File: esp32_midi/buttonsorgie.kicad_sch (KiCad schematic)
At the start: 199 parts, among them SW10 SW_SPST, SW11 SW_SPST, SW12 SW_SPST, SW13 SW_SPST, SW14 SW_SPST, SW15 SW_SPST, SW16 SW_SPST, SW17 SW_SPST, SW18 SW_SPST, SW19 SW_SPST, SW2 SW_SPST, SW20 SW_SPST, SW21 SW_SPST, SW22 SW_SPST, SW23 SW_SPST, SW24 SW_SPST, SW25 SW_SPST, SW26 SW_SPST, SW27 SW_SPST, SW28 SW_SPST, SW29 SW_SPST, SW3 SW_SPST, SW30 SW_SPST, SW31 SW_SPST, SW32 SW_SPST, SW33 SW_SPST, SW34 SW_SPST, SW35 SW_SPST, SW36 SW_SPST, SW37 SW_SPST, SW38 SW_SPST, SW39 SW_SPST, SW4 SW_SPST, SW40 SW_SPST, SW41 SW_SPST, SW42 SW_SPST, SW43 SW_SPST, SW44 SW_SPST, SW45 SW_SPST, SW46 SW_SPST, SW47 SW_SPST, SW48 SW_SPST, SW49 SW_SPST, SW5 SW_SPST, SW50 SW_SPST, SW51 SW_SPST, SW52 SW_SPST, SW53 SW_SPST, SW54 SW_SPST, SW55 SW_SPST, SW56 SW_SPST, SW57 SW_SPST, SW58 SW_SPST, SW59 SW_SPST, SW6 SW_SPST, SW60 SW_SPST, SW61 SW_SPST, SW62 SW_SPST, SW63 SW_SPST, SW64 SW_SPST, SW65 SW_SPST, SW7 SW_SPST, SW8 SW_SPST, SW9 SW_SPST

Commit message: Started work on PCB
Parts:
- added R48, R49, R50: 10k, Resistor_SMD:R_0402_1005Metric, symbol Device:R
- added SW66, SW67, SW68, SW69, SW70, SW71, SW72, SW73: SW_SPST, ordentliche-teile:scheißbutton, symbol Switch:SW_SPST
- added SW74, SW75, SW76, SW77: SW_SPST, ordentliche-teile:bobbybutton, symbol Switch:SW_SPST
- added SW78, SW79, SW80, SW81: SW_SPST, Connector_PinSocket_2.54mm:PinSocket_1x02_P2.54mm_Vertical, symbol Switch:SW_SPST
- added U? (x4): USBLC6-4SC6, Package_TO_SOT_SMD:SOT-23-6, symbol Power_Protection:USBLC6-4SC6
- added U? (x35): BL1551, Package_TO_SOT_SMD:SOT-363_SC-70-6, symbol Analog_Switch:FSA3157L6X
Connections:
- net +3.3V: now also R48.1, R49.1, R50.1, U?.5 (V+), U?.5 (V+), U?.5 (V+), U?.5 (V+), U?.5 (V+), U?.5 (V+), U?.5 (V+), U?.5 (V+), U?.5 (V+), U?.5 (V+), U?.5 (V+), U?.5 (V+), U?.5 (V+), U?.5 (V+), U?.5 (V+), U?.5 (V+), U?.5 (V+), U?.5 (V+), U?.5 (V+), U?.5 (V+)
- net +3V3: now also U?.5 (VBUS), U?.5 (VBUS), U?.5 (VBUS), U?.5 (VBUS)
- net GND: now also SW66.2 (B), SW67.2 (B), SW68.2 (B), SW69.2 (B), SW70.2 (B), SW71.2 (B), SW72.2 (B), SW73.2 (B), SW74.2 (B), SW75.2 (B), SW76.2 (B), SW77.2 (B), SW78.2 (B), SW79.2 (B), SW80.2 (B), SW81.2 (B), U?.2 (GND), U?.2 (GND), U?.2 (GND), U?.2 (GND), U?.2 (GND), U?.2 (GND), U?.2 (GND), U?.2 (GND), U?.2 (GND), U?.2 (GND), U?.2 (GND), U?.2 (GND), U?.2 (GND), U?.2 (GND), U?.2 (GND), U?.2 (GND), U?.2 (GND), U?.2 (GND), U?.2 (GND), U?.2 (GND), U?.2 (GND), U?.2 (GND), U?.2 (GND), U?.2 (GND)
- net OUTPUT0: now also R48.2
- net OUTPUT1: now also R49.2
- net SEL0: now also U?.6, U?.6, U?.6, U?.6, U?.6, U?.6, U?.6, U?.6
- net SEL1: now also U?.6, U?.6, U?.6, U?.6
- net SEL2: now also U?.6, U?.6
- net SEL3: now also U?.6
- new net: SW70.1 (A), U?.1 (I/O1), U?.3
- new net: SW71.1 (A), U?.1, U?.3 (I/O2)
- new net: SW73.1 (A), U?.1, U?.4 (I/O3)
- new net: SW72.1 (A), U?.3, U?.6 (I/O4)
- new net: SW80.1 (A), U?.3, U?.6 (I/O4)
- new net: SW76.1 (A), U?.3, U?.6 (I/O4)
- new net: SW67.1 (A), U?.1, U?.3 (I/O2)
- new net: SW66.1 (A), U?.1 (I/O1), U?.3
- new net: U?.3, U?.4 (x7)
- new net: U?.1, U?.4 (x7)
- new net: SW77.1 (A), U?.1, U?.4 (I/O3)
- new net: SW79.1 (A), U?.1, U?.3 (I/O2)
- new net: SW69.1 (A), U?.1, U?.4 (I/O3)
- new net: SW68.1 (A), U?.3, U?.6 (I/O4)
- new net: SW78.1 (A), U?.1 (I/O1), U?.3
- new net: SW81.1 (A), U?.1, U?.4 (I/O3)
- new net: SW75.1 (A), U?.1, U?.3 (I/O2)
- new net: SW74.1 (A), U?.1 (I/O1), U?.3
- new net OUTPUT2: R50.2, U?.4
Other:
- moved on the sheet: SW10, SW11, SW12, SW13, SW14, SW15, SW16, SW17, SW18, SW19, SW2, SW20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

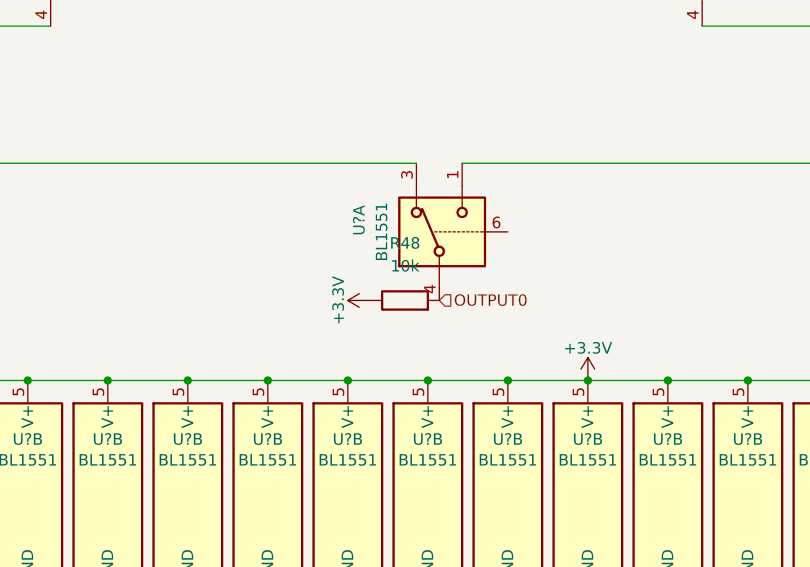
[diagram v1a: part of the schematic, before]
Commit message: More PCB implementations
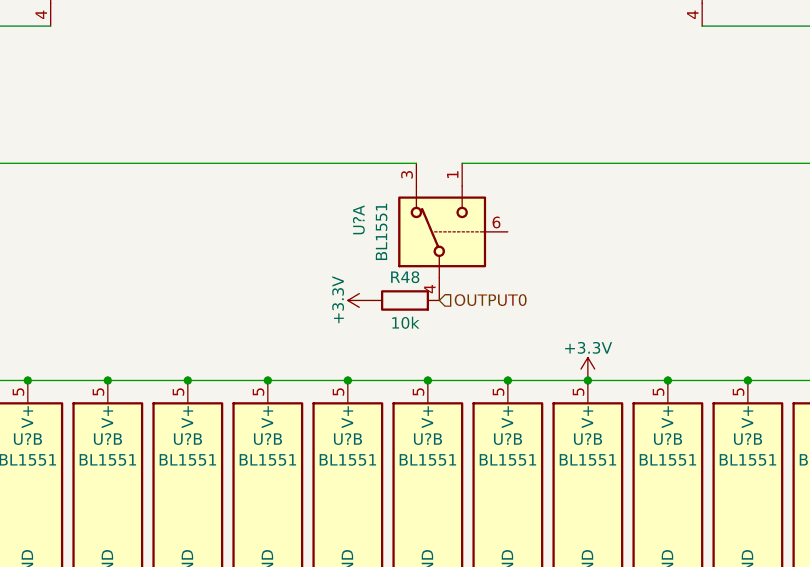
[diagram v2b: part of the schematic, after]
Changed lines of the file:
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@@
   (junction (at 345.44 273.05) (diameter 0) (color 0 0 0 0)
   )
+  (junction (at 402.59 148.59) (diameter 0) (color 0 0 0 0)
+  )
   (junction (at 527.05 63.5) (diameter 0) (color 0 0 0 0)
   )
@@
   (junction (at 518.16 173.99) (diameter 0) (color 0 0 0 0)
   )
-  (junction (at 402.59 148.59) (diameter 0) (color 0 0 0 0)
-  )
   (junction (at 218.44 63.5) (diameter 0) (color 0 0 0 0)
   )
@@
   (junction (at 144.78 148.59) (diameter 0) (color 0 0 0 0)
   )
+  (junction (at 402.59 173.99) (diameter 0) (color 0 0 0 0)
+  )
   (junction (at 349.25 148.59) (diameter 0) (color 0 0 0 0)
   )
@@
   (junction (at 162.56 148.59) (diameter 0) (color 0 0 0 0)
   )
-  (junction (at 402.59 173.99) (diameter 0) (color 0 0 0 0)
-  )
   (junction (at 411.48 148.59) (diameter 0) (color 0 0 0 0)
   )
@@
     (stroke (width 0) (type default))
   )
+  (wire (pts (xy 402.59 173.99) (xy 411.48 173.99))
+    (stroke (width 0) (type default))
+  )
   (wire (pts (xy 368.3 41.91) (xy 363.22 41.91))
     (stroke (width 0) (type default))
@@
     (stroke (width 0) (type default))
   )
-  (wire (pts (xy 402.59 173.99) (xy 411.48 173.99))
-    (stroke (width 0) (type default))
-  )
   (wire (pts (xy 220.98 26.67) (xy 227.33 26.67))
     (stroke (width 0) (type default))
@@
     (stroke (width 0) (type default))
   )
-  (wire (pts (xy 402.59 148.59) (xy 411.48 148.59))
-    (stroke (width 0) (type default))
-  )
   (wire (pts (xy 226.06 189.23) (xy 554.99 189.23))
     (stroke (width 0) (type default))
@@
     (stroke (width 0) (type default))
   )
+  (wire (pts (xy 402.59 148.59) (xy 411.48 148.59))
+    (stroke (width 0) (type default))
+  )
   (wire (pts (xy 251.46 41.91) (xy 251.46 63.5))
     (stroke (width 0) (type default))
@@
   )
   (symbol (lib_id "Device:R") (at 160.02 139.7 90) (unit 1)
-    (in_bom yes) (on_board yes) (dnp no) (fields_autoplaced)
-    (property "Reference" "R48" (at 160.02 133.35 90)
+    (in_bom yes) (on_board yes) (dnp no)
+    (property "Reference" "R48" (at 160.02 137.16 90)
       (effects (font (size 1.27 1.27)))
     )
-    (property "Value" "10k" (at 160.02 135.89 90)
+    (property "Value" "10k" (at 160.02 142.24 90)
       (effects (font (size 1.27 1.27)))
     )

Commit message: More pcb
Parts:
- R48, R49, R50: footprint Resistor_SMD:R_0402_1005Metric -> Resistor_SMD:R_1206_3216Metric
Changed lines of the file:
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@@
       (effects (font (size 1.27 1.27)))
     )
-    (property "Footprint" "Resistor_SMD:R_0402_1005Metric" (at 160.02 141.478 90)
+    (property "Footprint" "Resistor_SMD:R_1206_3216Metric" (at 160.02 141.478 90)
       (effects (font (size 1.27 1.27)) hide)
     )
@@
       (effects (font (size 1.27 1.27)))
     )
-    (property "Footprint" "Resistor_SMD:R_0402_1005Metric" (at 410.21 335.788 90)
+    (property "Footprint" "Resistor_SMD:R_1206_3216Metric" (at 410.21 335.788 90)
       (effects (font (size 1.27 1.27)) hide)
     )
@@
       (effects (font (size 1.27 1.27)))
     )
-    (property "Footprint" "Resistor_SMD:R_0402_1005Metric" (at 450.85 141.478 90)
+    (property "Footprint" "Resistor_SMD:R_1206_3216Metric" (at 450.85 141.478 90)
       (effects (font (size 1.27 1.27)) hide)
     )

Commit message: First load of bug fixes
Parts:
- U? (x154): footprint Package_TO_SOT_SMD:SOT-363_SC-70-6 -> Package_SON:Fairchild_MicroPak-6_1.0x1.45mm_P0.5mm
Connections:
- net +3V3 is gone; now on net +3.3V: U?.5 (VBUS), U?.5 (VBUS), U?.5 (VBUS), U?.5 (VBUS), U?.5 (VBUS), U?.5 (VBUS), U?.5 (VBUS), U?.5 (VBUS), U?.5 (VBUS), U?.5 (VBUS), U?.5 (VBUS), U?.5 (VBUS), U?.5 (VBUS), U?.5 (VBUS), U?.5 (VBUS), U?.5 (VBUS), U?.5 (VBUS), U?.5 (VBUS), U?.5 (VBUS), U?.5 (VBUS)
- net SEL4: now also U?.6

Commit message: Update parts numbers
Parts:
- R48, R49, R50, SW10, SW11, SW12, SW13, SW14, SW15, SW16, SW17, SW18, SW19, SW2, SW20, SW21, SW22, SW23, SW24, SW25, SW26, SW27, SW28, SW29, SW3, SW30, SW31, SW32, SW33, SW34, SW35, SW36, SW37, SW38, SW39, SW4, SW40, SW41, SW42, SW43, SW44, SW45, SW46, SW47, SW48, SW49, SW5, SW50, SW51, SW52, SW53, SW54, SW55, SW56, SW57, SW58, SW59, SW6, SW60, SW61, SW62, SW63, SW64, SW65, SW66, SW67, SW68, SW69, SW7, SW70, SW71, SW72, SW73, SW74, SW75, SW76, SW77, SW78, SW79, SW8, SW80, SW81, SW9, U? (x20): Field-1 (none) -> ${DNP}
- U? (x154): footprint Package_SON:Fairchild_MicroPak-6_1.0x1.45mm_P0.5mm -> Package_TO_SOT_SMD:SOT-363_SC-70-6; Field-1 (none) -> ${DNP}
